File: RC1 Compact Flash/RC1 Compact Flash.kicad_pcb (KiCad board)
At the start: 2 copper layers, 99.1 x 54.6 mm, 16 parts, among them J1 Expansion, J2 ADDRESS, J3 ADAPTER, J4 POWER, J5 POWER, U1 74LS00, U3 74LS138, U4 74LS138

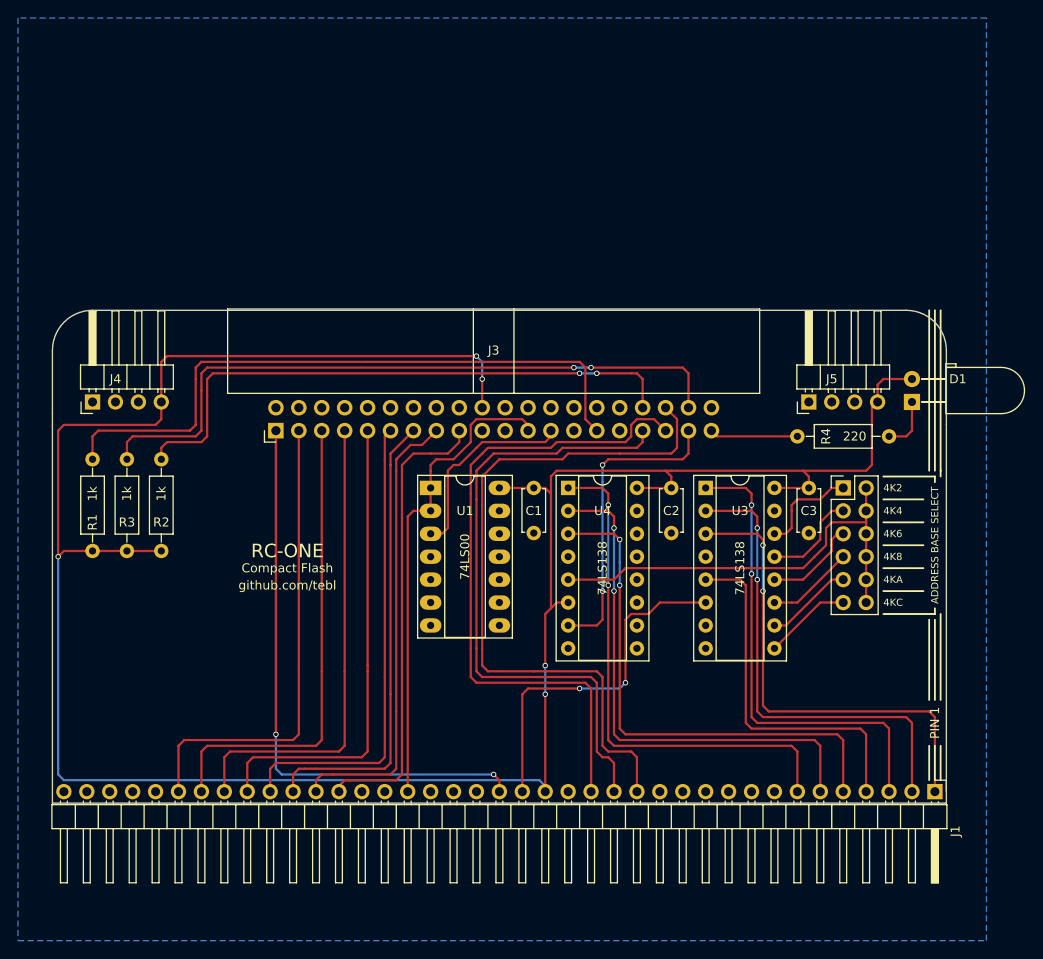
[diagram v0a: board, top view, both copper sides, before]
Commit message: Added buffer to Compact Flash
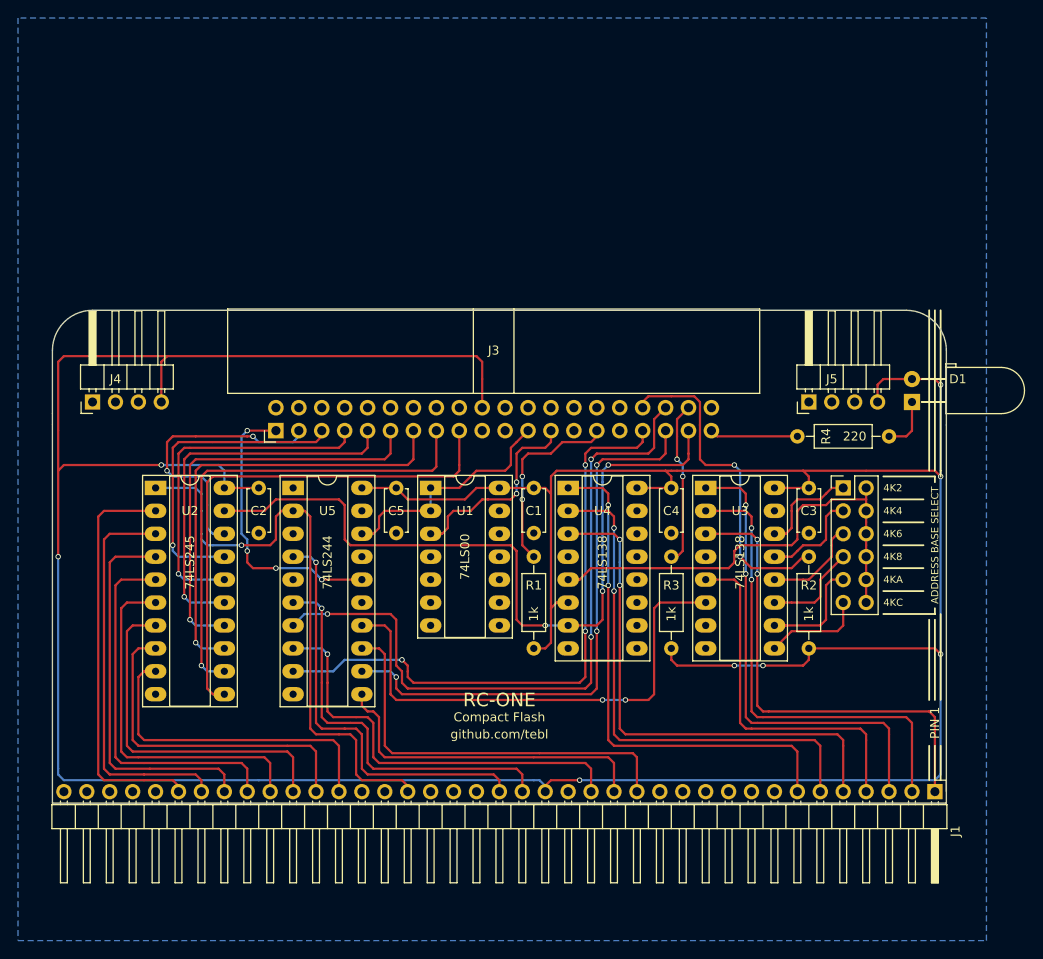
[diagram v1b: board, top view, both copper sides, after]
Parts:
- added C4: 100nF, Capacitors_THT:C_Disc_D4.7mm_W2.5mm_P5.00mm, F.Cu at (163.8, 113.7)
- added C5: 100nF, Capacitors_THT:C_Disc_D4.7mm_W2.5mm_P5.00mm, F.Cu at (133.3, 113.7)
- added U2: 74LS245, Housings_DIP:DIP-20_W7.62mm_Socket_LongPads, F.Cu at (106.7, 113.7)
- added U5: 74LS244, Housings_DIP:DIP-20_W7.62mm_Socket_LongPads, F.Cu at (121.9, 113.7)
- U3, U4: footprint Housings_DIP:DIP-16_W7.62mm_Socket -> Housings_DIP:DIP-16_W7.62mm_Socket_LongPads
- moved R2 72.6 mm to (179.1, 131.4)
- moved R3 61.3 mm to (163.8, 131.4)
- moved R1 50.1 mm to (148.6, 131.4)
- moved C2 45.7 mm to (118.1, 113.7)
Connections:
- J1 pad 14: /A2 -> Net-(J1-Pad14)
- J1 pad 15: /A1 -> Net-(J1-Pad15)
- J1 pad 16: /A0 -> Net-(J1-Pad16)
- J1 pad 19: /PHI2 -> Net-(J1-Pad19)
- J1 pad 20: /~RESET -> Net-(J1-Pad20)
- J1 pad 24: ~IOWR -> Net-(J1-Pad24)
- J1 pad 27: /D0 -> Net-(J1-Pad27)
- J1 pad 28: /D1 -> Net-(J1-Pad28)
- J1 pad 29: /D2 -> Net-(J1-Pad29)
- J1 pad 30: /D3 -> Net-(J1-Pad30)
- J1 pad 31: /D4 -> Net-(J1-Pad31)
- J1 pad 32: /D5 -> Net-(J1-Pad32)
- J1 pad 33: /D6 -> Net-(J1-Pad33)
- J1 pad 34: /D7 -> Net-(J1-Pad34)
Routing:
- net VCC: track 270.3 -> 416.2 mm, vias 5 -> 8
- net Net-(J1-Pad24): track 0.00 -> 65.9 mm, vias 0 -> 1
- net /CS1: track 75.3 -> 18.2 mm
- net ~CS_CF: track 33.8 -> 84.9 mm, vias 2 -> 3
- net Net-(J3-Pad29): track 72.1 -> 21.3 mm, vias 0 -> 2
- net Net-(J1-Pad16): track 0.00 -> 47.0 mm, vias 0 -> 1
- net Net-(J1-Pad20): track 0.00 -> 47.0 mm, vias 0 -> 1
- net Net-(J1-Pad14): track 0.00 -> 45.2 mm
- net Net-(J1-Pad34): track 0.00 -> 45.2 mm
- net Net-(J1-Pad19): track 0.00 -> 44.5 mm, vias 0 -> 1
- net Net-(J1-Pad33): track 0.00 -> 44.0 mm
- net Net-(J1-Pad32): track 0.00 -> 42.7 mm
- net Net-(J1-Pad31): track 0.00 -> 41.4 mm
- net Net-(J1-Pad30): track 0.00 -> 40.2 mm
- net Net-(J1-Pad29): track 0.00 -> 38.9 mm
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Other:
- board text added: "$2E00"
- board text added: "$4E00"
- board text added: "$6E00"
- board text added: "$8E00"
- board text added: "$AE00"
- board text added: "$CE00"
- board text added: "$CE00 $CE01 $CE02 $CE03"
- board text added: "$CE04 $CE05 $CE06 $CE07"
- board text added: "DATA BUFFER"
- board text added: "DATA ERROR (R), SET FEATURE (W) SECTORS LBA 0 (0-7)"
- board text added: "LBA 1 (8-15) LBA 2 (16-23) LBA 3 (24-27) STATUS (R), COMMAND (W)"
- board text added: "SIGNAL BUFFER"
- board text removed: "$3600"
- board text removed: "$5600"
- board text removed: "$7600"
- board text removed: "$9600"
- board text removed: "$B600"
- board text removed: "$D600"
